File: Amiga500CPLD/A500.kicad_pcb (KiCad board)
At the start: 2 copper layers, 54.9 x 110 mm, 12 parts, among them J1 Raspberry_Pi_2_3, U1 DeniseSocket, U2 DenisePins, U3 XC9572VQ44

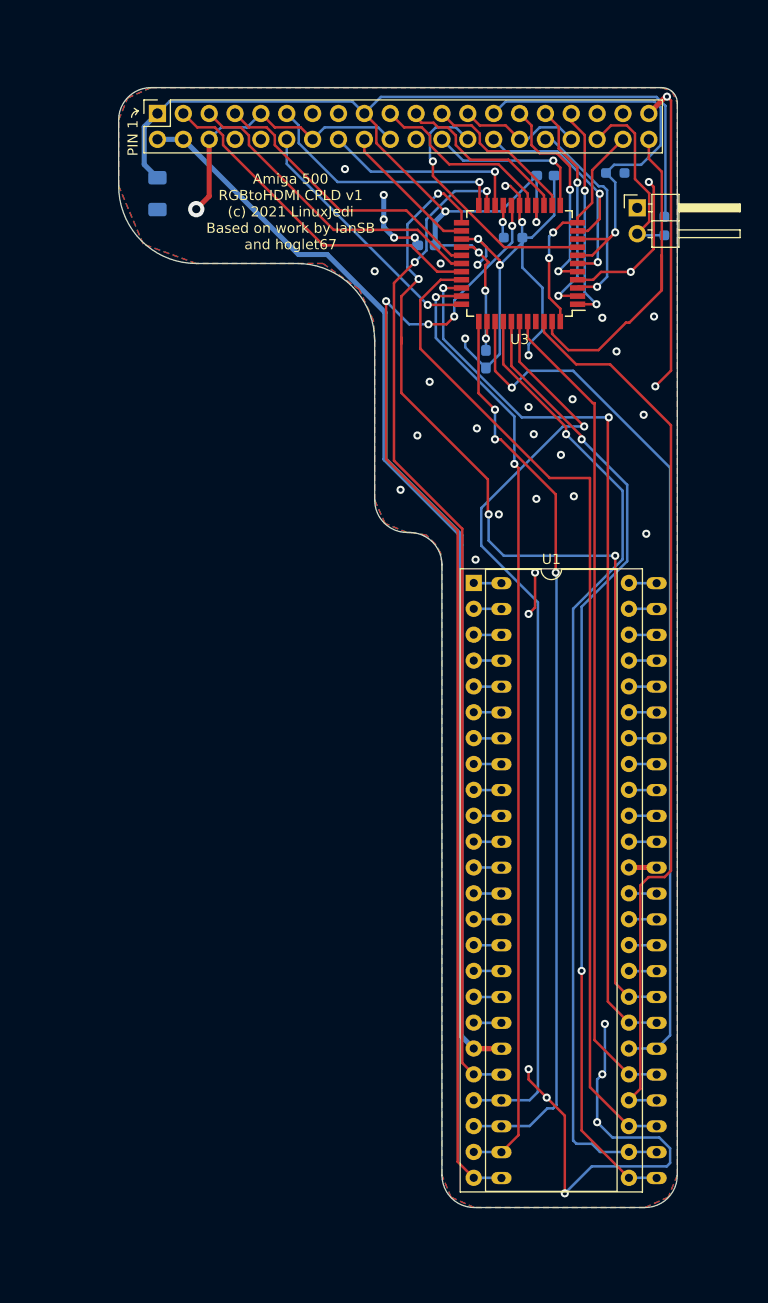
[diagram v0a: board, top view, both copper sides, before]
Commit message: Add Amiga 500 CPLD v2
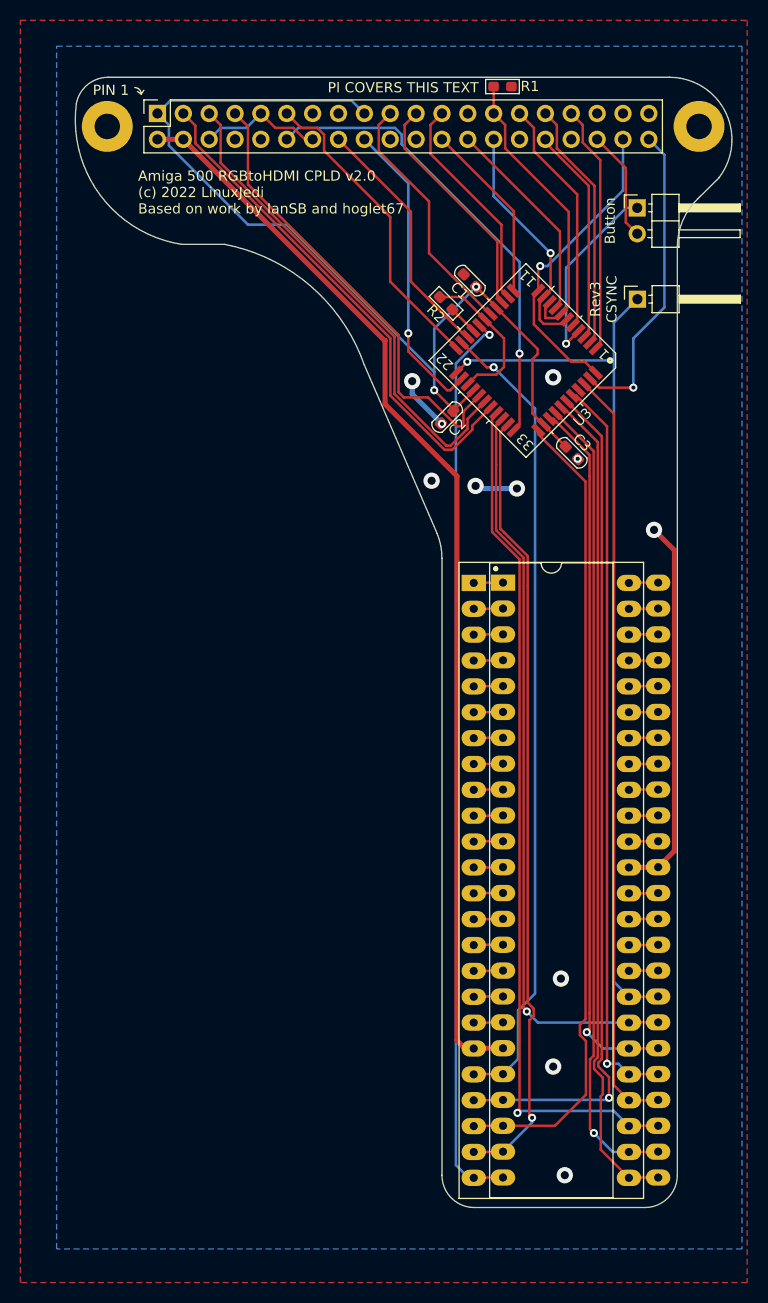
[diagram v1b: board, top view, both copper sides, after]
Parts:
- removed the C1 at (59.7, 30.7)
- removed the R1 at (109.5, 33.9)
- added H1: MountingHole, MountingHole:MountingHole_2.5mm_Pad, F.Cu at (112.9, 24.1)
- added H2: MountingHole, MountingHole:MountingHole_2.5mm_Pad, F.Cu at (54.8, 24.1)
- added J2: Conn_01x01, Connector_PinHeader_2.54mm:PinHeader_1x01_P2.54mm_Horizontal, F.Cu at (106.8, 41.1)
- C1: renamed from C2; footprint Capacitor_SMD:C_0603_1608Metric_Pad1.08x0.95mm_HandSolder -> Capacitor_SMD_AKL:C_0603_1608Metric_Pad1.08x0.95mm; moved to F.Cu
- C2: renamed from C3; footprint Capacitor_SMD:C_0603_1608Metric_Pad1.08x0.95mm_HandSolder -> Capacitor_SMD_AKL:C_0603_1608Metric_Pad1.08x0.95mm; moved to F.Cu
- C3: renamed from C4; footprint Capacitor_SMD:C_0603_1608Metric_Pad1.08x0.95mm_HandSolder -> Capacitor_SMD_AKL:C_0603_1608Metric_Pad1.08x0.95mm; moved to F.Cu
- R1: renamed from R2; footprint Resistor_SMD:R_0603_1608Metric_Pad0.98x0.95mm_HandSolder -> Resistor_SMD_AKL:R_0603_1608Metric_Pad1.05x0.95mm; moved to F.Cu
- R2: renamed from R3; footprint Resistor_SMD:R_0603_1608Metric_Pad0.98x0.95mm_HandSolder -> Resistor_SMD_AKL:R_0603_1608Metric_Pad1.05x0.95mm; moved to F.Cu
- U1: footprint Package_DIP:DIP-48_W15.24mm_Socket -> Package_DIP_AKL:DIP-48_W15.24mm_Socket_LongPads
- U2: footprint chips:DIP-48_pins -> Package_DIP_AKL:DIP-48_W15.24mm_LongPads; moved to F.Cu
- U3: footprint Package_QFP:TQFP-44_10x10mm_P0.8mm -> Package_QFP_AKL:TQFP-44_10x10mm_P0.8mm
- moved U2 27.6 mm to (93.6, 68.9), turned to 0 degrees
- moved C2 17.0 mm to (88.1, 52.7), turned to -135 degrees
- moved R1 14.0 mm to (93.6, 20.2)
- moved C1 12.7 mm to (90.4, 39.3), turned to 135 degrees
- moved C3 12.5 mm to (100.4, 56.2), turned to -45 degrees
- moved U3 9.55 mm to (95.9, 47.1), turned to -135 degrees
- moved R2 9.21 mm to (88.0, 41.5), turned to 135 degrees
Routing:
- net GND: track 200.4 -> 93.0 mm, vias 44 -> 12
- net +3V3: track 121.9 -> 97.6 mm, vias 5 -> 2
- net /B0: track 113.6 -> 89.8 mm, vias 4 -> 1
- net /GPIO18: track 25.3 -> 46.1 mm
- net /R0: track 99.7 -> 79.4 mm, vias 2 -> 1
- net /G2: track 87.7 -> 69.9 mm
- net /GPIO3: track 31.4 -> 48.4 mm
- net /GPIO4: track 28.6 -> 45.4 mm
- net /B2: track 96.0 -> 79.7 mm
- net /G3: track 89.3 -> 73.1 mm, vias 2 -> 1
- net /GPIO24: track 14.0 -> 29.9 mm, vias 0 -> 1
- net /R3: track 93.3 -> 77.4 mm, vias 2 -> 1
- net /GPIO2: track 34.3 -> 50.1 mm
- net /HSYNC: track 104.4 -> 89.0 mm, vias 4 -> 1
- net /B3: track 99.5 -> 84.6 mm, vias 0 -> 1
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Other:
- board size 54.9 x 110 mm -> 64.5 x 111 mm
- net class Default removed
- board text added: "Amiga 500 RGBtoHDMI CPLD v2.0 (c) 2022 LinuxJedi Based on work by IanSB and hoglet67"
- board text added: "Button"
- board text added: "PI COVERS THIS TEXT"
- board text added: "Rev3 CSYNC"
- board text removed: "Amiga 500 RGBtoHDMI CPLD v1 (c) 2021 LinuxJedi Based on work by IanSB and hoglet67"
